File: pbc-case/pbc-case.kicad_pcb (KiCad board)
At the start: 2 copper layers, 284 x 140.8 mm, 0 parts

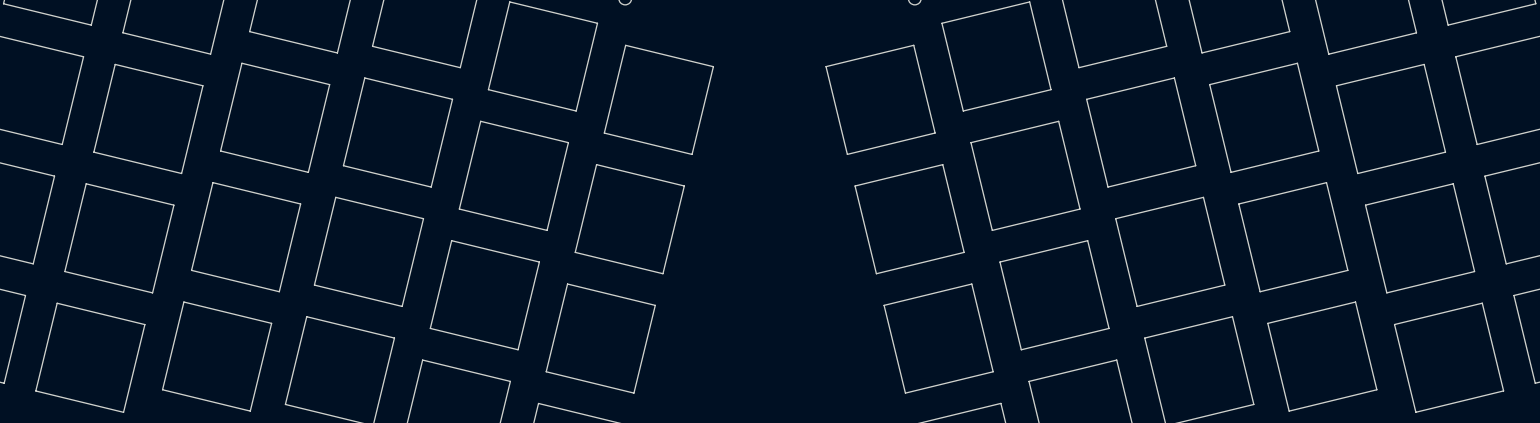
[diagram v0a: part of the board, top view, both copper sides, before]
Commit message: Added bottom side of the case. Rerouted some tracks to make space for the holes in the middle of the PCB. Added holes to the top case.
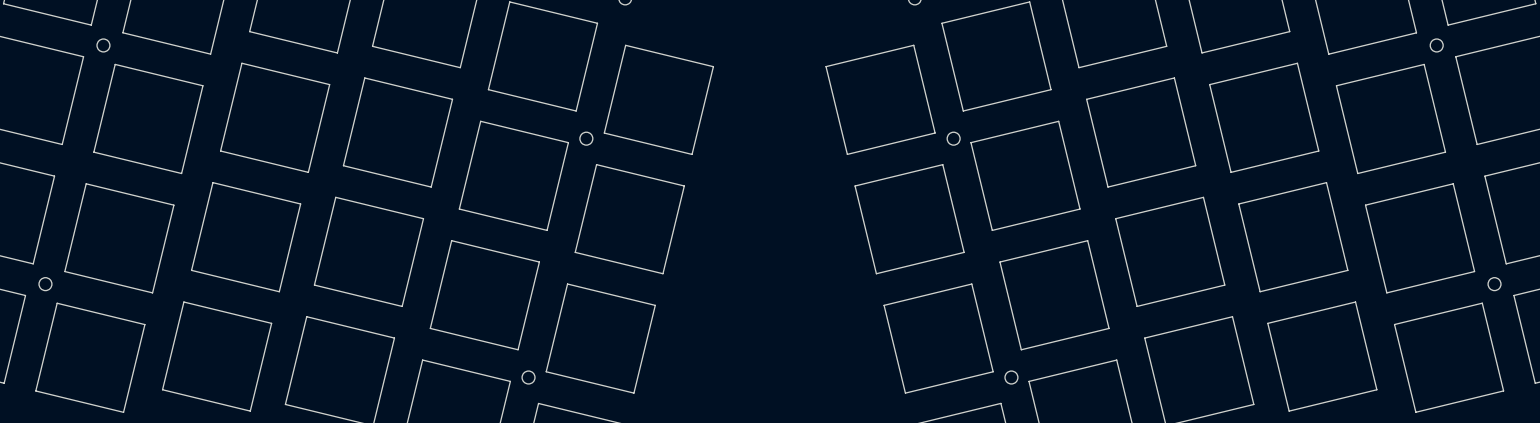
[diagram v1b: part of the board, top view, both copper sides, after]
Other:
- outline, holes or cut-outs redrawn
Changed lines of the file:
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@@
       (xy 151.746189 133.558607)
     ) (layer "Edge.Cuts") (width 0.15) (fill none))
+  (gr_circle (center 45.427402 51.887802) (end 46.227401 52.4878) (layer "Edge.Cuts") (width 0.1) (fill none))
   (gr_line (start 230.96 139.37) (end 230.9 139.63) (layer "Edge.Cuts") (width 0.1))
   (gr_line (start 230.95 138.13) (end 231 138.42) (layer "Edge.Cuts") (width 0.1))
@@
   (gr_line (start 289.56 107.52) (end 289.21 107.74) (layer "Edge.Cuts") (width 0.1))
   (gr_line (start 192.17 31.87) (end 195.55 30.51) (layer "Edge.Cuts") (width 0.1))
+  (gr_circle (center 120.306602 66.340402) (end 121.106601 66.9404) (layer "Edge.Cuts") (width 0.1) (fill none))
   (gr_line (start 79.8 146.92) (end 77.52 145.89) (layer "Edge.Cuts") (width 0.1))
   (gr_circle (center 227.18 138.33) (end 227.98 138.93) (layer "Edge.Cuts") (width 0.1) (fill none))
@@
   (gr_line (start 69.66 125.39) (end 69.67 125.1) (layer "Edge.Cuts") (width 0.1))
   (gr_line (start 143.02 163.41) (end 138.36 163.1) (layer "Edge.Cuts") (width 0.1))
+  (gr_circle (center 36.435802 88.895602) (end 37.235801 89.4956) (layer "Edge.Cuts") (width 0.1) (fill none))
   (gr_poly
     (pts
@@
   (gr_line (start 224.84 143.64) (end 221.87 145.04) (layer "Edge.Cuts") (width 0.1))
   (gr_line (start 206.76 151.5) (end 204.29 152.43) (layer "Edge.Cuts") (width 0.1))
+  (gr_circle (center 177.253402 66.340402) (end 178.053401 66.9404) (layer "Edge.Cuts") (width 0.1) (fill none))
   (gr_line (start 246.15 22.62) (end 252.52 22.61) (layer "Edge.Cuts") (width 0.1))
   (gr_line (start 177.51 37.3) (end 182.45 35.69) (layer "Edge.Cuts") (width 0.1))
@@
   (gr_line (start 227.9 125.39) (end 227.95 125.71) (layer "Edge.Cuts") (width 0.1))
   (gr_line (start 120.05 37.3) (end 125.63 38.71) (layer "Edge.Cuts") (width 0.1))
+  (gr_circle (center 111.340402 103.373602) (end 112.140401 103.9736) (layer "Edge.Cuts") (width 0.1) (fill none))
   (gr_line (start 67.49 122.19) (end 9.48 108.14) (layer "Edge.Cuts") (width 0.1))
   (gr_line (start 120.8 160.55) (end 118.14 159.98) (layer "Edge.Cuts") (width 0.1))
@@
       (xy 65.353422 39.628612)
     ) (layer "Edge.Cuts") (width 0.15) (fill none))
+  (gr_circle (center 261.124202 88.895602) (end 261.924201 89.4956) (layer "Edge.Cuts") (width 0.1) (fill none))
   (gr_line (start 63.76 23.05) (end 68.77 23.39) (layer "Edge.Cuts") (width 0.1))
   (gr_poly
@@
   (gr_line (start 228.16 123.82) (end 228.05 124.1) (layer "Edge.Cuts") (width 0.1))
   (gr_line (start 200.72 28.63) (end 206.18 27.01) (layer "Edge.Cuts") (width 0.1))
+  (gr_circle (center 252.158002 51.887802) (end 252.958001 52.4878) (layer "Edge.Cuts") (width 0.1) (fill none))
   (gr_line (start 229.03 141.62) (end 224.84 143.64) (layer "Edge.Cuts") (width 0.1))
   (gr_line (start 26.2 24.87) (end 26.34 24.53) (layer "Edge.Cuts") (width 0.1))
@@
       (xy 230.563422 54.651388)
     ) (layer "Edge.Cuts") (width 0.15) (fill none))
-  (gr_poly
-    (pts
+  (gr_circle (center 186.219602 103.373602) (end 187.019601 103.9736) (layer "Edge.Cuts") (width 0.1) (fill none))
+  (gr_poly
+    (pts
